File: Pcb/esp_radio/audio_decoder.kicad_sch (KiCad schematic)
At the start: 34 parts, among them U4 VS1053, Y1 12.288Mhz

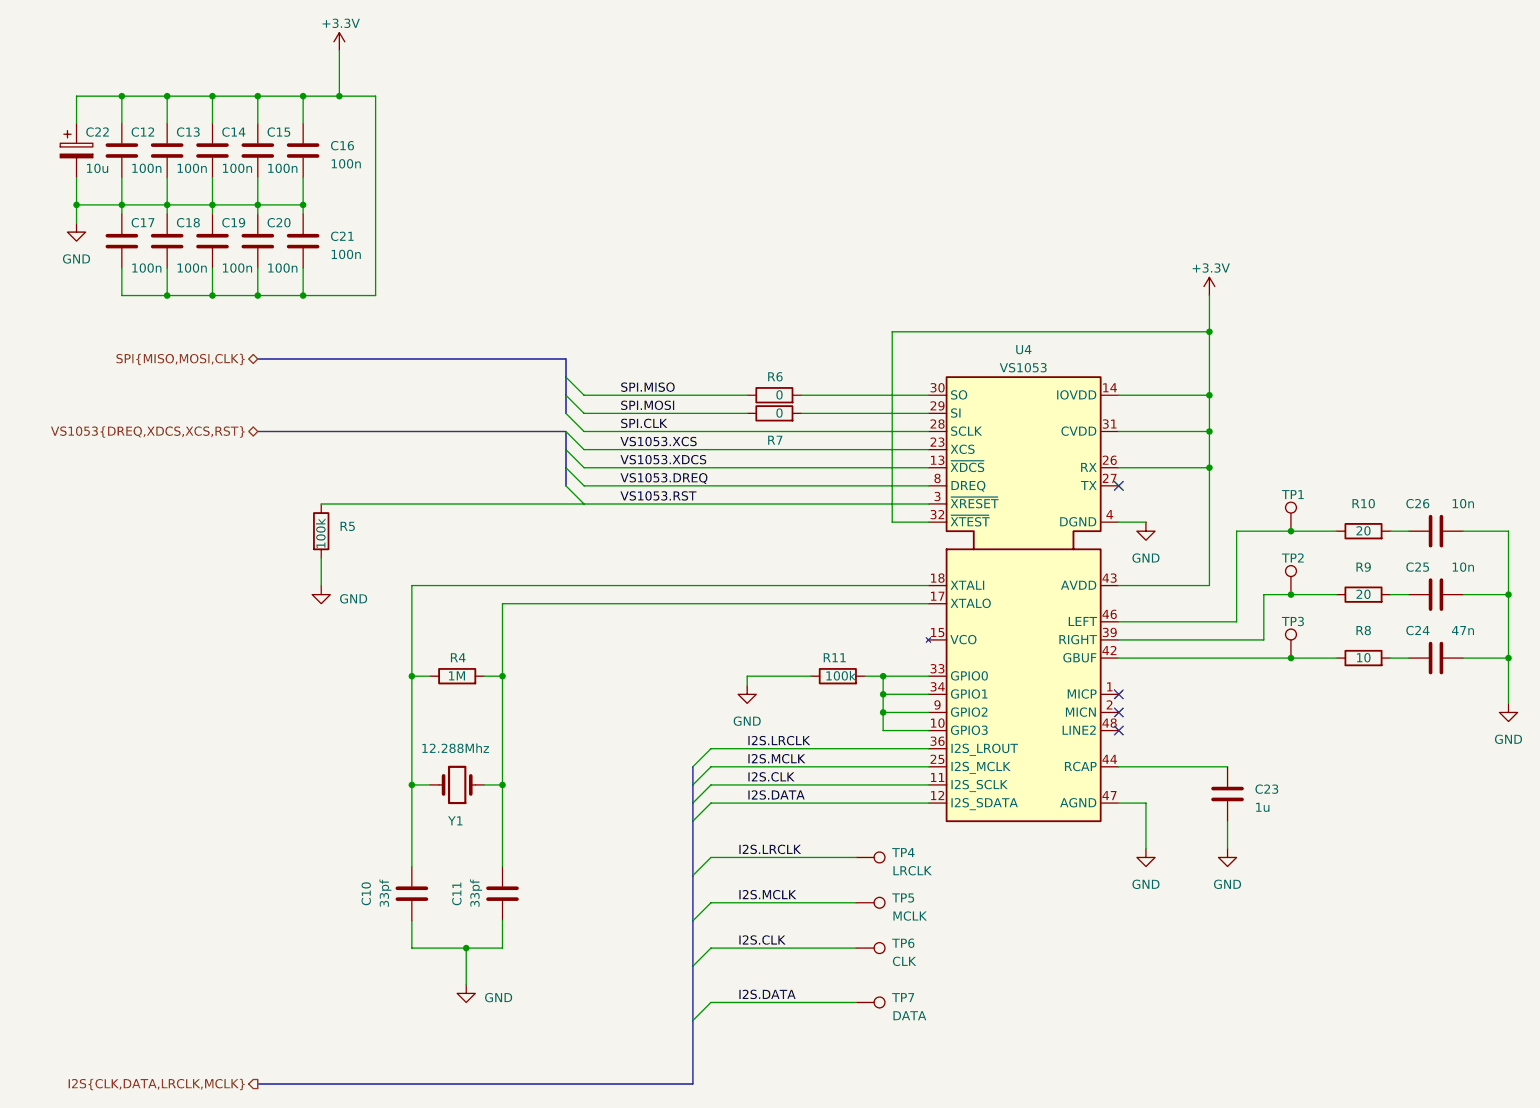
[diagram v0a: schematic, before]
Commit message: Move custom components to kicad_common_library.
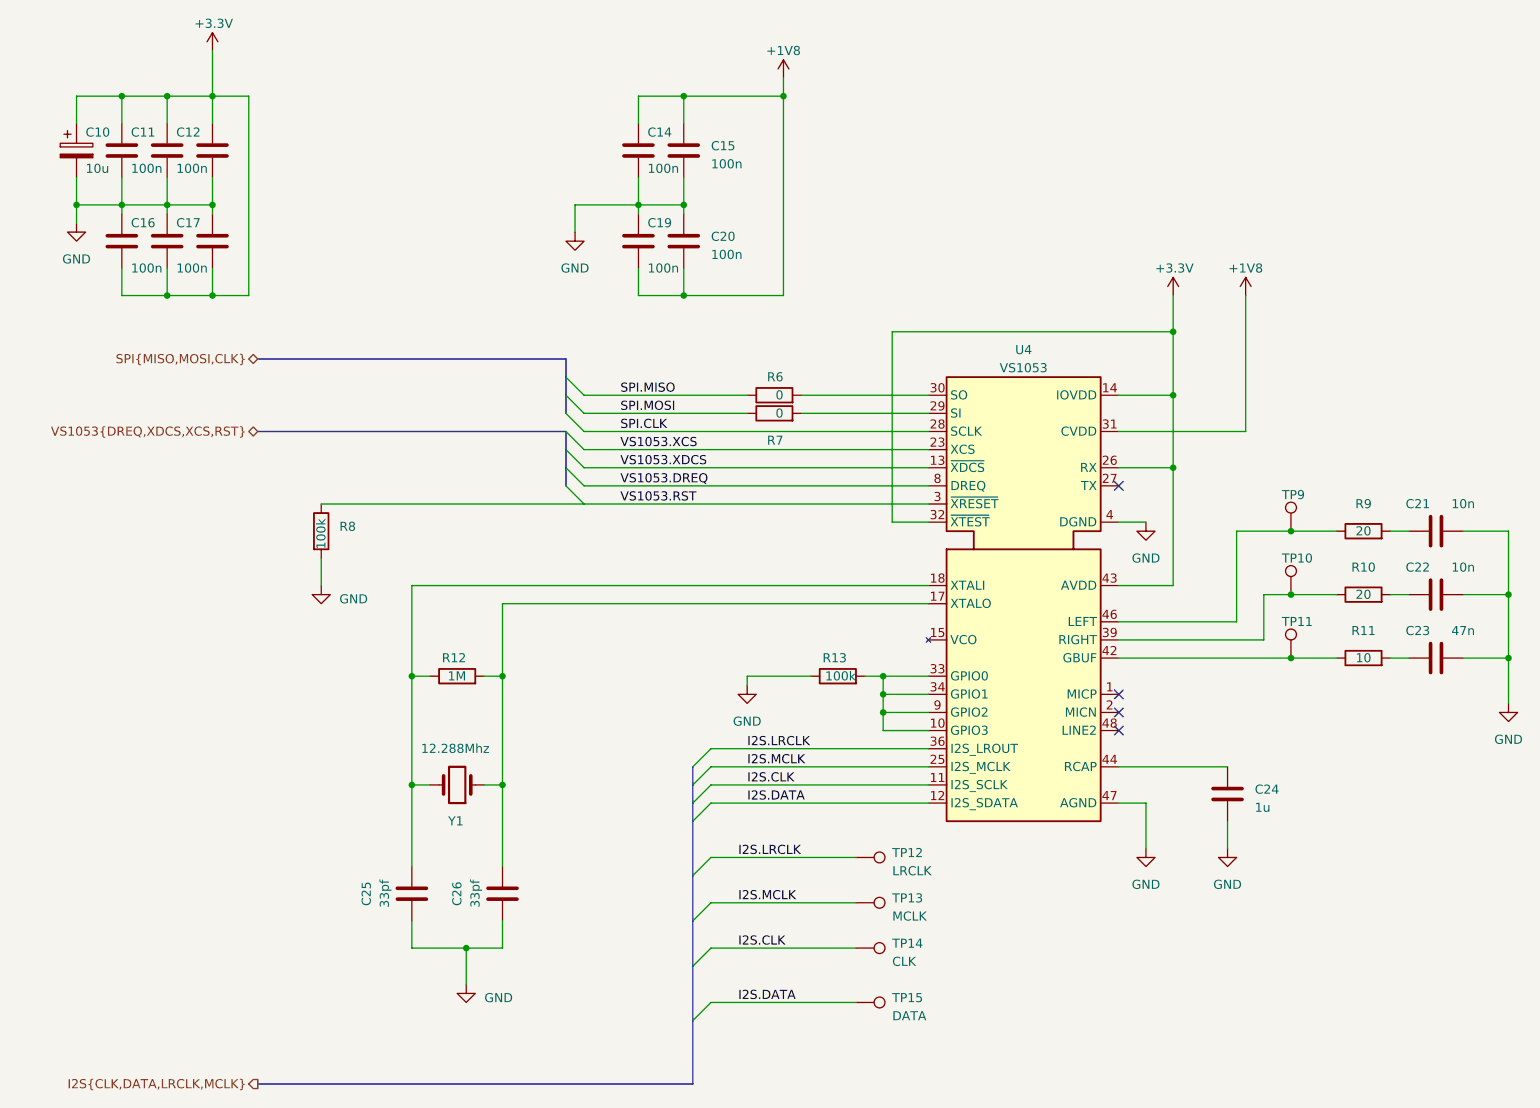
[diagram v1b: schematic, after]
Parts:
- removed C16, C21: 100n, symbol Device:C
- added C14, C19: 100n, symbol Device:C
- U4: symbol vs1053:VS1053 -> kicad_common_lib:VS1053
- renumbered C22 to C10, C12 to C11, C13 to C12, C14 to C13, C17 to C16, C18 to C17, C19 to C18, C26 to C21, C25 to C22, C24 to C23, C23 to C24, C10 to C25, C11 to C26, R9 to R10, R8 to R11, R4 to R12, R11 to R13, R5 to R8, R10 to R9, TP2 to TP10, TP3 to TP11, TP4 to TP12, TP5 to TP13, TP6 to TP14, TP7 to TP15, TP1 to TP9
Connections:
- net +3.3V: no longer C15.2, C20.1, U4.24 (CVDD), U4.31 (CVDD), U4.5 (CVDD), U4.7 (CVDD)
- net AGND: now also C14.1, C19.2
- new net +1V8: C14.2, C15.2, C19.1, C20.1, U4.24 (CVDD), U4.31 (CVDD), U4.5 (CVDD), U4.7 (CVDD)

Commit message: Add components layout on PCB
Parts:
- C10: footprint (none) -> Capacitor_THT:CP_Radial_D5.0mm_P2.50mm
- C11, C12, C13, C14, C15, C16, C17, C18, C19, C20, C21, C22, C23, C24, C25, C26: footprint (none) -> kicad_common_lib:C_0805
- R10, R11, R12, R13, R6, R7, R8, R9: footprint (none) -> kicad_common_lib:R_0805
- TP10, TP11, TP12, TP13, TP14, TP15, TP9: footprint (none) -> TestPoint:TestPoint_THTPad_D2.0mm_Drill1.0mm
- Y1: footprint (none) -> Crystal:Crystal_HC18-U_Vertical
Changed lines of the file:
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@@
       (effects (font (size 1.27 1.27)) (justify right))
     )
-    (property "Footprint" "" (at 96.8248 40.64 0)
+    (property "Footprint" "kicad_common_lib:C_0805" (at 96.8248 40.64 0)
       (effects (font (size 1.27 1.27)) hide)
     )
@@
       (effects (font (size 1.27 1.27)) (justify right))
     )
-    (property "Footprint" "" (at 30.7848 40.64 0)
+    (property "Footprint" "kicad_common_lib:C_0805" (at 30.7848 40.64 0)
       (effects (font (size 1.27 1.27)) hide)
     )
@@
       (effects (font (size 1.27 1.27)) (justify left))
     )
-    (property "Footprint" "" (at 128.27 156.21 0)
+    (property "Footprint" "TestPoint:TestPoint_THTPad_D2.0mm_Drill1.0mm" (at 128.27 156.21 0)
       (effects (font (size 1.27 1.27)) hide)
     )
@@
       (effects (font (size 1.27 1.27)))
     )
-    (property "Footprint" "" (at 199.39 95.758 90)
+    (property "Footprint" "kicad_common_lib:R_0805" (at 199.39 95.758 90)
       (effects (font (size 1.27 1.27)) hide)
     )
@@
       (effects (font (size 1.27 1.27)))
     )
-    (property "Footprint" "" (at 199.39 86.868 90)
+    (property "Footprint" "kicad_common_lib:R_0805" (at 199.39 86.868 90)
       (effects (font (size 1.27 1.27)) hide)
     )
@@
       (effects (font (size 1.27 1.27)))
     )
-    (property "Footprint" "" (at 65.0748 132.08 0)
+    (property "Footprint" "kicad_common_lib:C_0805" (at 65.0748 132.08 0)
       (effects (font (size 1.27 1.27)) hide)
     )
@@
       (effects (font (size 1.27 1.27)) (justify right) hide)
     )
-    (property "Footprint" "" (at 37.1348 40.64 0)
+    (property "Footprint" "kicad_common_lib:C_0805" (at 37.1348 40.64 0)
       (effects (font (size 1.27 1.27)) hide)
     )
@@
       (effects (font (size 1.27 1.27)))
     )
-    (property "Footprint" "" (at 199.39 104.648 90)
+    (property "Footprint" "kicad_common_lib:R_0805" (at 199.39 104.648 90)
       (effects (font (size 1.27 1.27)) hide)
     )
@@
       (effects (font (size 1.27 1.27)) (justify right))
     )
-    (property "Footprint" "" (at 24.4348 27.94 0)
+    (property "Footprint" "kicad_common_lib:C_0805" (at 24.4348 27.94 0)
       (effects (font (size 1.27 1.27)) hide)
     )
@@
       (effects (font (size 1.27 1.27)) (justify right))
     )
-    (property "Footprint" "" (at 30.7848 27.94 0)
+    (property "Footprint" "kicad_common_lib:C_0805" (at 30.7848 27.94 0)
       (effects (font (size 1.27 1.27)) hide)
     )
@@
       (effects (font (size 1.27 1.27)) (justify right))
     )
-    (property "Footprint" "" (at 96.8248 27.94 0)
+    (property "Footprint" "kicad_common_lib:C_0805" (at 96.8248 27.94 0)
       (effects (font (size 1.27 1.27)) hide)
     )
@@
       (effects (font (size 1.27 1.27)) (justify left) hide)
     )
-    (property "Footprint" "" (at 194.31 93.98 0)
+    (property "Footprint" "TestPoint:TestPoint_THTPad_D2.0mm_Drill1.0mm" (at 194.31 93.98 0)
       (effects (font (size 1.27 1.27)) hide)
     )
@@
       (effects (font (size 1.27 1.27)))
     )
-    (property "Footprint" "" (at 213.36 93.0148 0)
+    (property "Footprint" "kicad_common_lib:C_0805" (at 213.36 93.0148 0)
       (effects (font (size 1.27 1.27)) hide)
     )
@@
       (effects (font (size 1.27 1.27)) (justify left))
     )
-    (property "Footprint" "" (at 116.84 70.358 90)
+    (property "Footprint" "kicad_common_lib:R_0805" (at 116.84 70.358 90)
       (effects (font (size 1.27 1.27)) hide)
     )
@@
       (effects (font (size 1.27 1.27)) (justify right))
     )
-    (property "Footprint" "" (at 103.1748 40.64 0)
+    (property "Footprint" "kicad_common_lib:C_0805" (at 103.1748 40.64 0)
       (effects (font (size 1.27 1.27)) hide)
     )
@@
       (effects (font (size 1.27 1.27)) (justify right) hide)
     )
-    (property "Footprint" "" (at 37.1348 27.94 0)
+    (property "Footprint" "kicad_common_lib:C_0805" (at 37.1348 27.94 0)
       (effects (font (size 1.27 1.27)) hide)
     )
@@
       (effects (font (size 1.27 1.27)) (justify right))
     )
-    (property "Footprint" "" (at 179.3748 118.11 0)
+    (property "Footprint" "kicad_common_lib:C_0805" (at 179.3748 118.11 0)
       (effects (font (size 1.27 1.27)) hide)
     )
@@
       (effects (font (size 1.27 1.27)))
     )
-    (property "Footprint" "" (at 213.36 101.9048 0)
+    (property "Footprint" "kicad_common_lib:C_0805" (at 213.36 101.9048 0)
       (effects (font (size 1.27 1.27)) hide)
     )
@@
       (effects (font (size 1.27 1.27)) (justify left))
     )
-    (property "Footprint" "" (at 128.27 148.59 0)
+    (property "Footprint" "TestPoint:TestPoint_THTPad_D2.0mm_Drill1.0mm" (at 128.27 148.59 0)
       (effects (font (size 1.27 1.27)) hide)
     )
@@
       (effects (font (size 1.27 1.27)) (justify left))
     )
-    (property "Footprint" "" (at 72.39 107.188 90)
+    (property "Footprint" "kicad_common_lib:R_0805" (at 72.39 107.188 90)
       (effects (font (size 1.27 1.27)) hide)
     )
@@
       (effects (font (size 1.27 1.27)) (justify left))
     )
-    (property "Footprint" "" (at 128.27 142.24 0)
+    (property "Footprint" "TestPoint:TestPoint_THTPad_D2.0mm_Drill1.0mm" (at 128.27 142.24 0)
       (effects (font (size 1.27 1.27)) hide)
     )
@@
       (effects (font (size 1.27 1.27)) (justify left))
     )
-    (property "Footprint" "" (at 20.0152 35.56 0)
+    (property "Footprint" "Capacitor_THT:CP_Radial_D5.0mm_P2.50mm" (at 20.0152 35.56 0)
       (effects (font (size 1.27 1.27)) hide)
     )
@@
       (effects (font (size 1.27 1.27)))
     )
-    (property "Footprint" "" (at 213.36 84.1248 0)
+    (property "Footprint" "kicad_common_lib:C_0805" (at 213.36 84.1248 0)
       (effects (font (size 1.27 1.27)) hide)
     )
@@
       (effects (font (size 1.27 1.27)) (justify left) hide)
     )
-    (property "Footprint" "" (at 194.31 102.87 0)
+    (property "Footprint" "TestPoint:TestPoint_THTPad_D2.0mm_Drill1.0mm" (at 194.31 102.87 0)
       (effects (font (size 1.27 1.27)) hide)
     )
@@
       (effects (font (size 1.27 1.27)) (justify left))
     )
-    (property "Footprint" "" (at 128.27 135.89 0)
+    (property "Footprint" "TestPoint:TestPoint_THTPad_D2.0mm_Drill1.0mm" (at 128.27 135.89 0)
       (effects (font (size 1.27 1.27)) hide)
     )
@@
       (effects (font (size 1.27 1.27)) (justify left) hide)
     )
-    (property "Footprint" "" (at 194.31 85.09 0)
+    (property "Footprint" "TestPoint:TestPoint_THTPad_D2.0mm_Drill1.0mm" (at 194.31 85.09 0)
       (effects (font (size 1.27 1.27)) hide)
     )
@@
       (effects (font (size 1.27 1.27)) (justify left))
     )
-    (property "Footprint" "" (at 116.84 67.818 90)
+    (property "Footprint" "kicad_common_lib:R_0805" (at 116.84 67.818 90)
       (effects (font (size 1.27 1.27)) hide)
     )
@@
       (effects (font (size 1.27 1.27)) (justify left))
     )
-    (property "Footprint" "" (at 125.73 107.188 90)
+    (property "Footprint" "kicad_common_lib:R_0805" (at 125.73 107.188 90)
       (effects (font (size 1.27 1.27)) hide)
     )
@@
       (effects (font (size 1.27 1.27)) (justify right))
     )
-    (property "Footprint" "" (at 24.4348 40.64 0)
+    (property "Footprint" "kicad_common_lib:C_0805" (at 24.4348 40.64 0)
       (effects (font (size 1.27 1.27)) hide)
     )
@@
       (effects (font (size 1.27 1.27)) (justify right))
     )
-    (property "Footprint" "" (at 103.1748 27.94 0)
+    (property "Footprint" "kicad_common_lib:C_0805" (at 103.1748 27.94 0)
       (effects (font (size 1.27 1.27)) hide)
     )
@@
       (effects (font (size 1.27 1.27)))
     )
-    (property "Footprint" "" (at 79.7052 139.7 0)
+    (property "Footprint" "kicad_common_lib:C_0805" (at 79.7052 139.7 0)
       (effects (font (size 1.27 1.27)) hide)
     )
@@
       (effects (font (size 1.27 1.27)) (justify right))
     )
-    (property "Footprint" "" (at 72.39 120.65 0)
+    (property "Footprint" "Crystal:Crystal_HC18-U_Vertical" (at 72.39 120.65 0)
       (effects (font (size 1.27 1.27)) hide)
     )
@@
       (effects (font (size 1.27 1.27)) (justify left))
     )
-    (property "Footprint" "" (at 51.562 85.09 90)
-      (effects (font (size 1.27 1.27)) hide)
-    )
+    (property "Footprint" "kicad_common_lib:R_0805" (at 51.562 85.09 90)
+      (effects (font (size 1.27 1.27)) hide)
+    )
